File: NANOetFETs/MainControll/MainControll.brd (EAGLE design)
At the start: 80 x 48.3 mm, 17 parts

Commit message: 1st prototype
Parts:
- added JP1: (no value), pinhead:1X04
- FET_AIRPUMP, FET_COLLECTPUMP, FET_VALVE, FET_WATERPUMP: value IRF740 -> 2SK2232; device transistor-power:TO220BV -> Transistor-FET:TO220
- moved FET_COLLECTPUMP 5.34 mm to (66.8, 22.5)
- moved FET_AIRPUMP 5.34 mm to (66.8, 42.8)
- moved FET_VALVE 5.34 mm to (66.8, 32.6)
- moved FET_WATERPUMP 5.34 mm to (66.8, 12.3)
- moved TERMINAL_WATERPUMP 5.34 mm to (79.5, 9.75)
- moved TERMINAL_AIRPUMP 5.34 mm to (79.5, 40.2)
- moved TERMINAL_COLLECTPUMP 5.34 mm to (79.5, 19.9)
- moved TERMINAL_VALVE 5.34 mm to (79.5, 30.1)
- moved SW_LED 3.25 mm to (14.0, 7.11)
- moved R4 2.54 mm to (24.1, 41.9)
- moved C1 2.54 mm to (38.1, 16.5)
- moved R1 2.54 mm to (29.2, 41.9)
- moved R2 2.54 mm to (26.7, 41.9)
- moved R3 2.54 mm to (21.6, 41.9)
- moved U$2 2.54 mm to (21.6, 29.2)
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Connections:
- new net N$1: JP1.3, U$2.RX1
- new net N$2: JP1.2, U$2.TX0
- net +12V: now also JP1.1
- net AIRPUMP: now also FET_AIRPUMP.1; no longer FET_AIRPUMP.G
- net COLPUMP: now also FET_COLLECTPUMP.1; no longer FET_COLLECTPUMP.G
- net GND: now also FET_AIRPUMP.3, FET_COLLECTPUMP.3, FET_VALVE.3, FET_WATERPUMP.3, JP1.4; no longer FET_AIRPUMP.S, FET_COLLECTPUMP.S, FET_VALVE.S, FET_WATERPUMP.S
- net N$10: now also FET_COLLECTPUMP.2; no longer FET_COLLECTPUMP.D
- net N$7: now also FET_AIRPUMP.2; no longer FET_AIRPUMP.D
- net N$8: now also FET_VALVE.2; no longer FET_VALVE.D
- net N$9: now also FET_WATERPUMP.2; no longer FET_WATERPUMP.D
- net VALVE: now also FET_VALVE.1; no longer FET_VALVE.G
- net WATPUMP: now also FET_WATERPUMP.1; no longer FET_WATERPUMP.G
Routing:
- net +12V: track 140.5 -> 216.6 mm
- net AIRPUMP: track 39.0 -> 55.4 mm
- net N$2: track 0.00 -> 13.5 mm
- net N$1: track 0.00 -> 13.5 mm
- net WATPUMP: track 56.1 -> 66.4 mm
- net VALVE: track 44.5 -> 53.9 mm
- net COLPUMP: track 50.2 -> 58.6 mm
- net N$10: track 11.2 -> 7.40 mm
- net N$8: track 11.2 -> 7.40 mm
- net N$7: track 11.2 -> 7.40 mm
- net N$9: track 11.2 -> 7.40 mm
- net +5V: track 17.7 -> 15.5 mm
- net N$14: track 16.5 -> 14.5 mm
- net N$13: track 16.5 -> 14.5 mm
- net N$12: track 16.5 -> 14.5 mm
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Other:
- board size 80 x 48.3 mm -> 85 x 55 mm

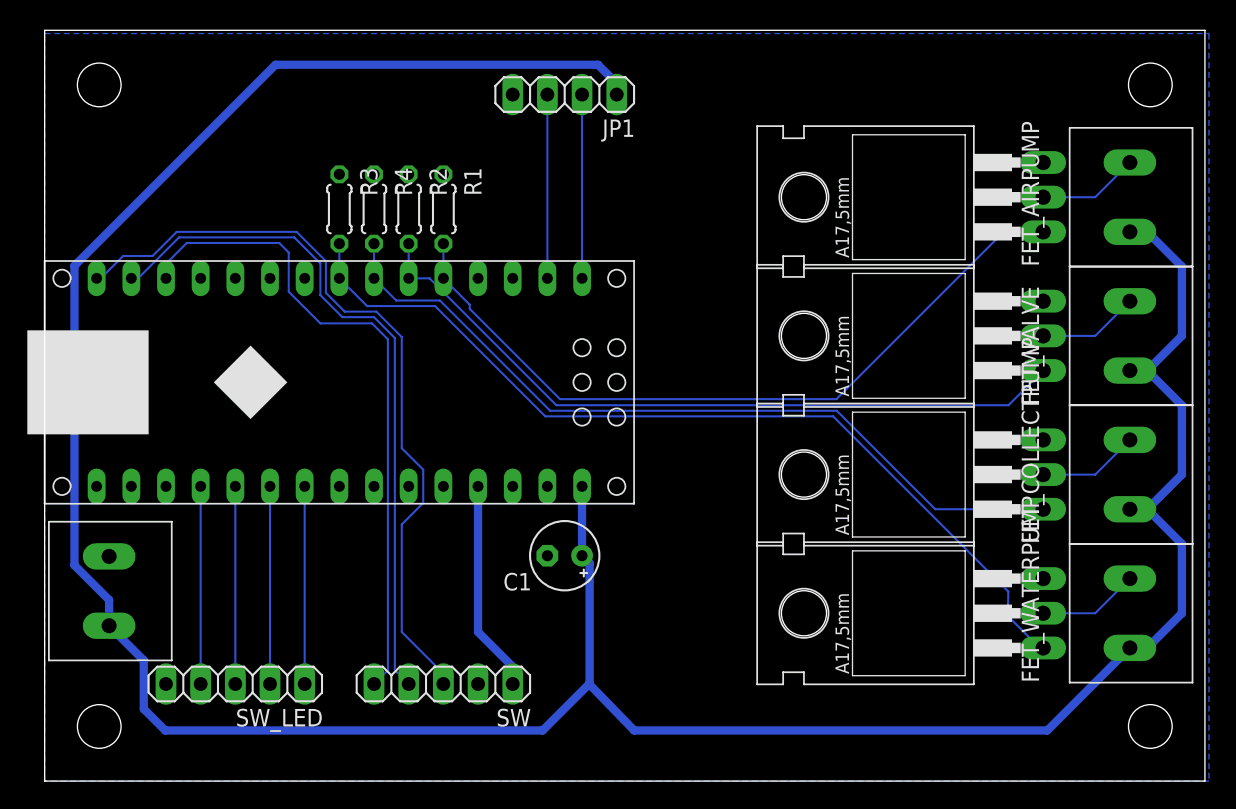
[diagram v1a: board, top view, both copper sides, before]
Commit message: Re-routed some signals to fix errors of clearance; Added Gerber files and a Mit file; Added git-ignore setting file
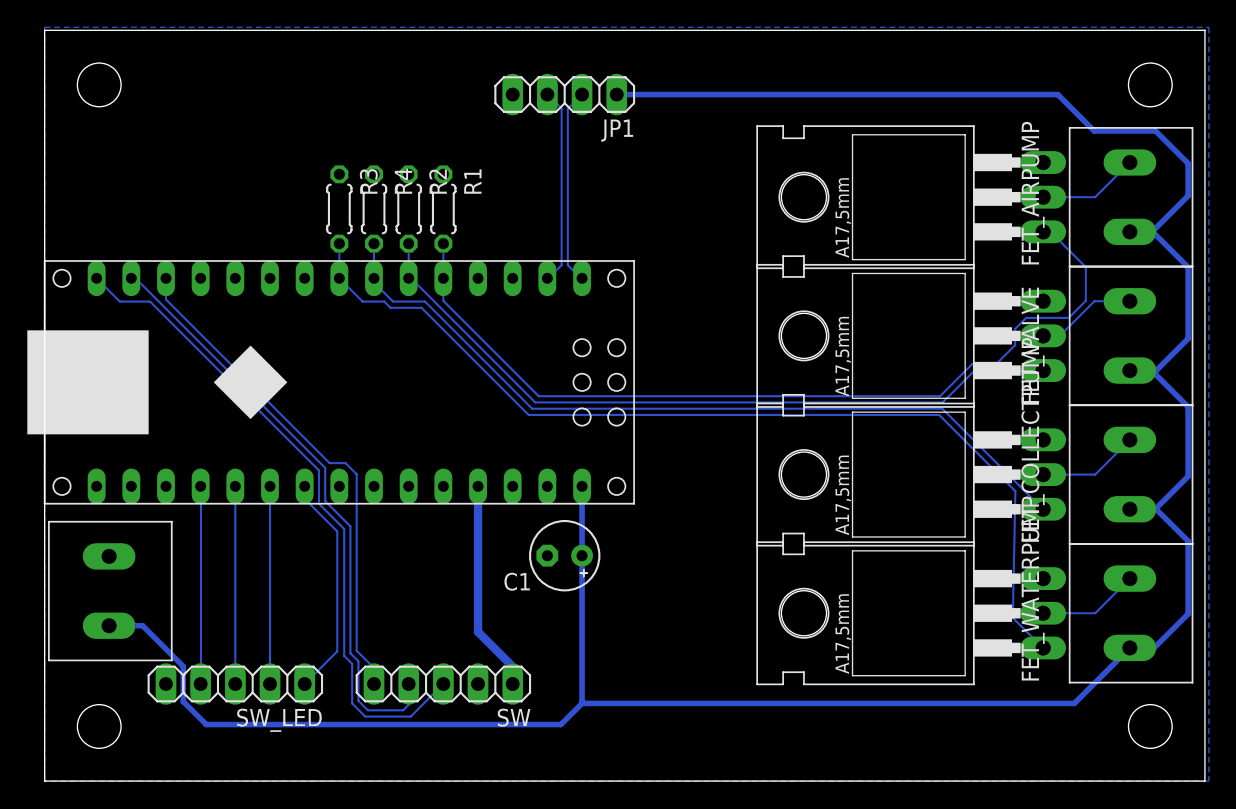
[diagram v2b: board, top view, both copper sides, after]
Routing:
- net +12V: track 216.6 -> 197.0 mm
- net SW1: track 48.2 -> 36.7 mm
- net AIRPUMP: track 55.4 -> 64.4 mm
- net SW3: track 56.3 -> 48.3 mm
- net SW2: track 50.8 -> 43.7 mm
- net WATPUMP: track 66.4 -> 71.4 mm
- net N$14: track 14.5 -> 16.5 mm
- net N$1: track 13.5 -> 14.4 mm
- net N$2: track 13.5 -> 14.4 mm

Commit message: brd手直し
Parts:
- moved FET_AIRPUMP 4.68 mm to (64.8, 47.0)
- moved FET_WATERPUMP 3.96 mm to (64.8, 8.89)
- moved FET_VALVE 2.63 mm to (64.8, 34.3)
- moved FET_COLLECTPUMP 2.21 mm to (64.8, 21.6)
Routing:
- net GND: track 0.00 -> 211.6 mm
- net SW2: track 43.7 -> 88.7 mm
- net +12V: track 197.0 -> 164.8 mm, vias 0 -> 1
- net COLPUMP: track 58.7 -> 90.6 mm
- net SW1: track 36.7 -> 56.3 mm, vias 0 -> 1
- net +5V: track 15.5 -> 34.0 mm
- net AIRPUMP: track 64.4 -> 46.6 mm, vias 0 -> 1
- net SW3: track 48.3 -> 56.9 mm, vias 0 -> 1
- net WATPUMP: track 71.4 -> 65.1 mm
- net VALVE: track 53.8 -> 49.5 mm
- net N$9: track 7.40 -> 10.9 mm
- net N$10: track 7.40 -> 9.83 mm
- net N$14: track 16.5 -> 14.5 mm
- net N$7: track 7.40 -> 9.21 mm
- net N$8: track 7.40 -> 8.78 mm
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- added copper zone on layer 1, net GND
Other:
- outline, holes or cut-outs redrawn
